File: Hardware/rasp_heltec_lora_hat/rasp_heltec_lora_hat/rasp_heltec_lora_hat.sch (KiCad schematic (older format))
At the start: 18 parts, among them J1 Conn_I2C_1, J2 Conn_I2C_2, J3 CONN_DAC2, J4 Conn_Alim, J5 Con_ADC1, P1 Conn_02x20_Odd_Even, U1 Heltec_Wifi_LoRa_V1

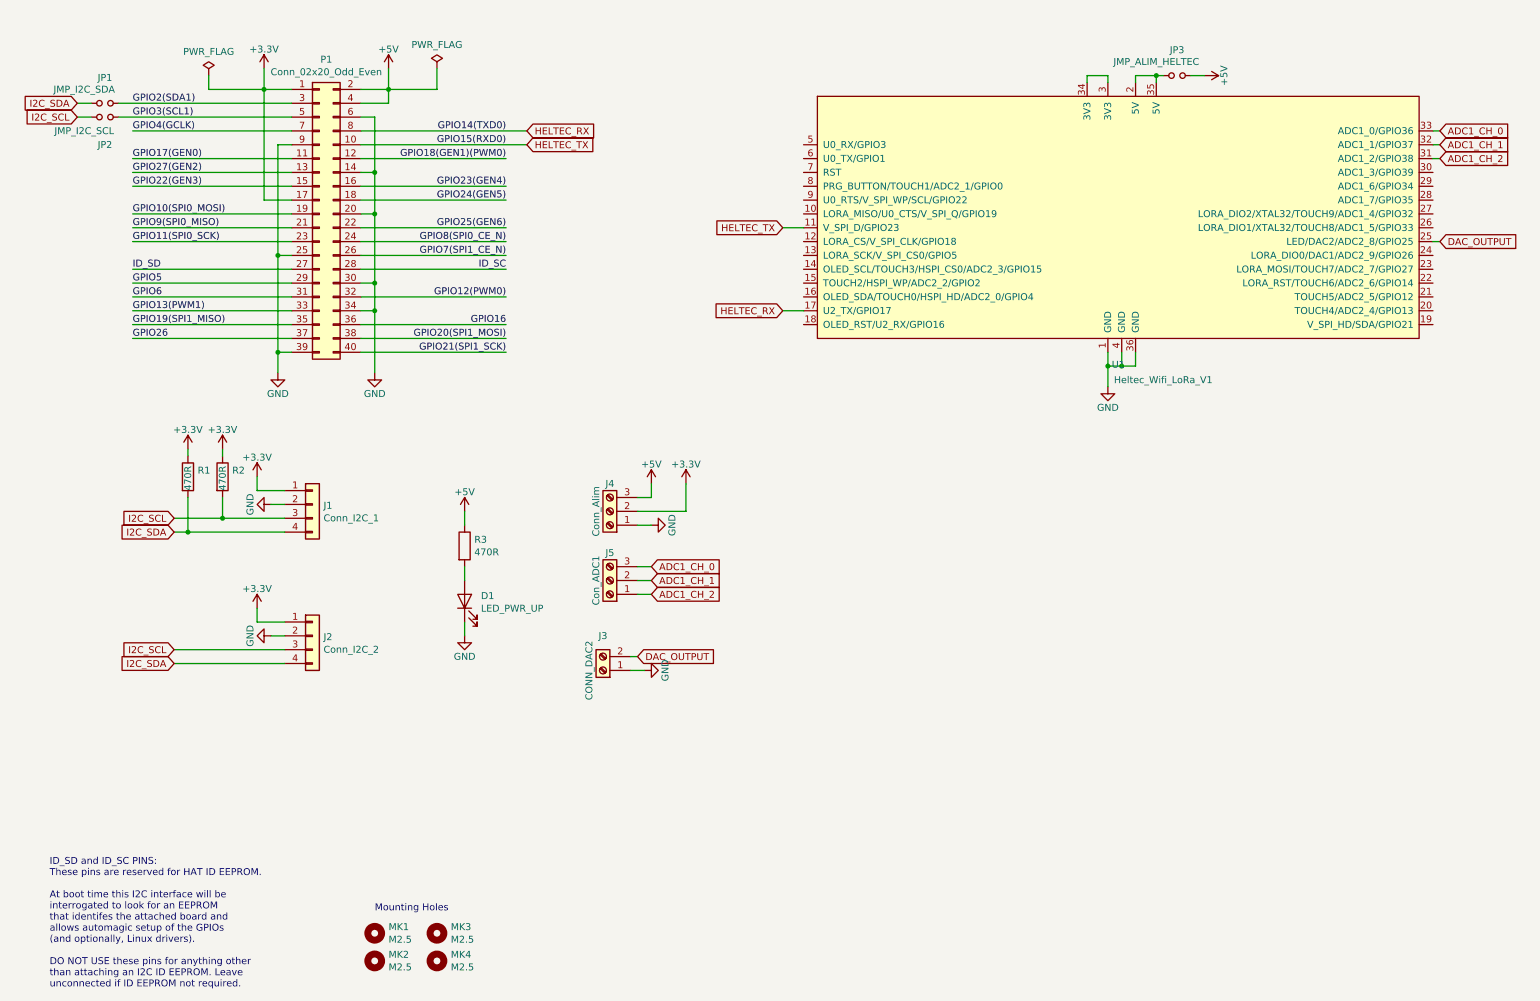
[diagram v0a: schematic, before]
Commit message: Atualizações de hardware:
- Atualizada placa para uso com versão 2 do Heltec LoRa
- Adicionado diodo 1N5819 para permitir funcionamento e programação simultaneos
- Invertidos os conectores I2C para comportar módulos pequenos (exemplo: BMP180) conectaos diretamente na placa
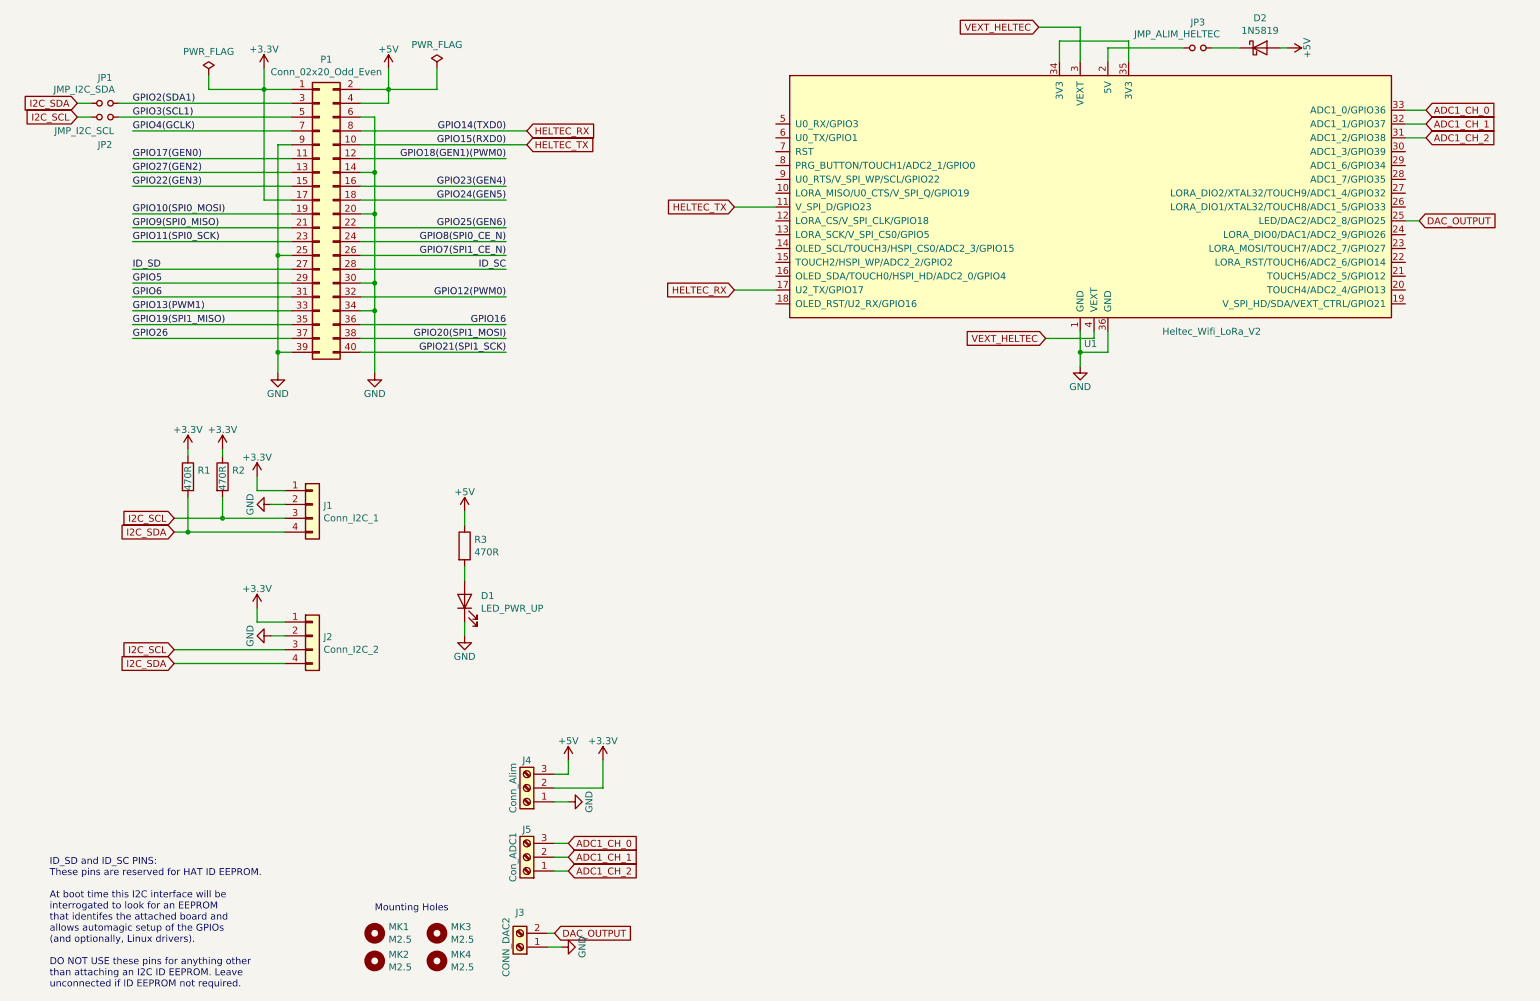
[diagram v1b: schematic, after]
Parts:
- removed U1: Heltec_Wifi_LoRa_V1, heltec_wifi_lora_v1:Heltec_WiFi_LoRa_V1, symbol heltec_wifi_lora_v1:Heltec_Wifi_LoRa_V1
- added D2: 1N5819, Diode_THT:D_DO-41_SOD81_P10.16mm_Horizontal, symbol Diode:1N5819
- added U1: Heltec_Wifi_LoRa_V2, heltec_wifi_lora_V2:Heltec_WiFi_LoRa_V2, symbol heltec_wifi_lora_v2:Heltec_Wifi_LoRa_V2
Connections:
- net +5V: now also D2.2 (A); no longer JP3.2
- net ADC1_CH_0: now also U1.33 (ADC1_0/GPIO36)
- net ADC1_CH_1: now also U1.32 (ADC1_1/GPIO37)
- net ADC1_CH_2: now also U1.31 (ADC1_2/GPIO38)
- net DAC_OUTPUT: now also U1.25 (LED/DAC2/ADC2_8/GPIO25)
- net GND: now also U1.1 (GND), U1.36 (GND)
- net HELTEC_RX: now also U1.17 (U2_TX/GPIO17)
- net HELTEC_TX: now also U1.11 (V_SPI_D/GPIO23)
- net at JP3.1: now also U1.2 (5V)
- new net: U1.34 (3V3), U1.35 (3V3)
- new net: D2.1 (K), JP3.2
- new net VEXT_HELTEC: U1.3 (VEXT), U1.4 (VEXT)
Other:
- moved on the sheet: J3, J4, J5
